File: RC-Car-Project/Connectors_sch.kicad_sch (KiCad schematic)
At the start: 9 parts, among them J1 XT60-M, J2 XT60-M, J3 XT60-M, J4 XT60-M, J5 MCU_IF, J6 ANT_IF, J7 Conn_02x09_Odd_Even

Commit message: Started on the PCB
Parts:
- removed J1, J2, J3, J4: XT60-M, symbol XT60-M:XT60-M
- added J1, J2, J3, J4: Conn_01x02_Pin, Connector_AMASS:AMASS_XT60-M_1x02_P7.20mm_Vertical, symbol Connector:Conn_01x02_Pin
- added J10, J8, J9: Conn_01x02, Connector_JST:JST_XH_B2B-XH-AM_1x02_P2.50mm_Vertical, symbol Connector_Generic:Conn_01x02
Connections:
- net GND_BATT: now also J1.1 (Pin_1), J2.1 (Pin_1)
- net LIGHTS1_NEG: now also J8.2 (Pin_2)
- net LIGHTS1_POS: now also J8.1 (Pin_1)
- net LIGHTS2_NEG: now also J9.2 (Pin_2)
- net LIGHTS2_POS: now also J9.1 (Pin_1)
- net M1_LEFT: now also J4.1 (Pin_1)
- net M1_RIGHT: now also J4.2 (Pin_2)
- net M2_LEFT: now also J3.1 (Pin_1)
- net M2_RIGHT: now also J3.2 (Pin_2)
- net THERMO1: now also J10.1 (Pin_1)
- net THERMO2: now also J10.2 (Pin_2)
- net VDD_BATT: now also J1.2 (Pin_2), J2.2 (Pin_2)

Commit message: Fixed Drivers
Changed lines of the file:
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@@
-		)
-	)
-	(hierarchical_label "RELAY_CTRL"
-		(shape input)
-		(at 196.85 86.36 180)
-		(fields_autoplaced yes)
-		(effects
-			(font
-				(size 1.27 1.27)
-			)
-			(justify right)
 		)
 	)

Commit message: Fixed Annotations
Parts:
- R3: renamed from R26; footprint Resistor_SMD:R_0201_0603Metric -> Resistor_SMD:R_0603_1608Metric
- R4: renamed from R25; footprint Resistor_SMD:R_0201_0603Metric -> Resistor_SMD:R_0603_1608Metric
- renumbered J6 to J10, J8 to J6, J9 to J7, J10 to J8, J7 to J9
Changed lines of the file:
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@@
 		(on_board yes)
 		(dnp no)
-		(property "Reference" "#PWR0104"
+		(property "Reference" "#PWR018"
 			(at 142.24 40.64 0)
 			(effects
@@
 			(project "RC-Car-Project"
 				(path "/ba870fd1-751d-4755-8e1a-1ea86ca9e2f6/47812da9-b622-4bda-8507-4e09448e1ff5"
-					(reference "#PWR0104")
+					(reference "#PWR018")
 					(unit 1)
 				)
@@
 		(dnp no)
 		(fields_autoplaced yes)
-		(property "Reference" "#PWR09"
+		(property "Reference" "#PWR015"
 			(at 127 92.71 0)
 			(effects
@@
 			(project "RC-Car-Project"
 				(path "/ba870fd1-751d-4755-8e1a-1ea86ca9e2f6/47812da9-b622-4bda-8507-4e09448e1ff5"
-					(reference "#PWR09")
+					(reference "#PWR015")
 					(unit 1)
 				)
@@
 		(on_board yes)
 		(dnp no)
-		(property "Reference" "#PWR012"
+		(property "Reference" "#PWR017"
 			(at 144.78 77.47 0)
 			(effects
@@
 			(project "RC-Car-Project"
 				(path "/ba870fd1-751d-4755-8e1a-1ea86ca9e2f6/47812da9-b622-4bda-8507-4e09448e1ff5"
-					(reference "#PWR012")
+					(reference "#PWR017")
 					(unit 1)
 				)
@@
 		(dnp no)
 		(fields_autoplaced yes)
-		(property "Reference" "J10"
+		(property "Reference" "J8"
 			(at 137.16 138.4299 0)
 			(effects
@@
 			(project "RC-Car-Project"
 				(path "/ba870fd1-751d-4755-8e1a-1ea86ca9e2f6/47812da9-b622-4bda-8507-4e09448e1ff5"
-					(reference "J10")
+					(reference "J8")
 					(unit 1)
 				)
@@
 		(dnp no)
 		(fields_autoplaced yes)
-		(property "Reference" "#PWR095"
+		(property "Reference" "#PWR014"
 			(at 67.31 104.14 0)
 			(effects
@@
 			(project "RC-Car-Project"
 				(path "/ba870fd1-751d-4755-8e1a-1ea86ca9e2f6/47812da9-b622-4bda-8507-4e09448e1ff5"
-					(reference "#PWR095")
+					(reference "#PWR014")
 					(unit 1)
 				)
@@
 		(dnp no)
 		(fields_autoplaced yes)
-		(property "Reference" "#PWR013"
+		(property "Reference" "#PWR020"
 			(at 165.1 67.31 0)
 			(effects
@@
 			(project "RC-Car-Project"
 				(path "/ba870fd1-751d-4755-8e1a-1ea86ca9e2f6/47812da9-b622-4bda-8507-4e09448e1ff5"
-					(reference "#PWR013")
+					(reference "#PWR020")
 					(unit 1)
 				)
@@
 		(dnp no)
 		(fields_autoplaced yes)
-		(property "Reference" "#PWR0105"
+		(property "Reference" "#PWR019"
 			(at 157.48 40.64 0)
 			(effects
@@
 			(project "RC-Car-Project"
 				(path "/ba870fd1-751d-4755-8e1a-1ea86ca9e2f6/47812da9-b622-4bda-8507-4e09448e1ff5"
-					(reference "#PWR0105")
+					(reference "#PWR019")
 					(unit 1)
 				)
@@
 		(dnp no)
 		(fields_autoplaced yes)
-		(property "Reference" "J8"
+		(property "Reference" "J6"
 			(at 137.16 123.1899 0)
 			(effects
@@
 			(project ""
 				(path "/ba870fd1-751d-4755-8e1a-1ea86ca9e2f6/47812da9-b622-4bda-8507-4e09448e1ff5"
-					(reference "J8")
+					(reference "J6")
 					(unit 1)
 				)
@@
 		(dnp no)
 		(fields_autoplaced yes)
-		(property "Reference" "J7"
+		(property "Reference" "J9"
 			(at 154.94 34.29 0)
 			(effects
@@
 			(project ""
 				(path "/ba870fd1-751d-4755-8e1a-1ea86ca9e2f6/47812da9-b622-4bda-8507-4e09448e1ff5"
-					(reference "J7")
+					(reference "J9")
 					(unit 1)
 				)
@@
 		(dnp no)
 		(fields_autoplaced yes)
-		(property "Reference" "#PWR08"
+		(property "Reference" "#PWR016"
 			(at 116.84 95.25 0)
 			(effects
@@
 			(project "RC-Car-Project"
 				(path "/ba870fd1-751d-4755-8e1a-1ea86ca9e2f6/47812da9-b622-4bda-8507-4e09448e1ff5"
-					(reference "#PWR08")
+					(reference "#PWR016")
 					(unit 1)
 				)
@@
 		(dnp no)
 		(fields_autoplaced yes)
-		(property "Reference" "#PWR092"
+		(property "Reference" "#PWR011"
 			(at 77.47 92.71 0)
 			(effects
@@
 			(project "RC-Car-Project"
 				(path "/ba870fd1-751d-4755-8e1a-1ea86ca9e2f6/47812da9-b622-4bda-8507-4e09448e1ff5"
-					(reference "#PWR092")
+					(reference "#PWR011")
 					(unit 1)
 				)
@@
 		(dnp no)
 		(fields_autoplaced yes)
-		(property "Reference" "#PWR094"
+		(property "Reference" "#PWR013"
 			(at 77.47 101.6 0)
 			(effects
@@
 			(project "RC-Car-Project"
 				(path "/ba870fd1-751d-4755-8e1a-1ea86ca9e2f6/47812da9-b622-4bda-8507-4e09448e1ff5"
-					(reference "#PWR094")
+					(reference "#PWR013")
 					(unit 1)
 				)
@@
 		(dnp no)
 		(fields_autoplaced yes)
-		(property "Reference" "#PWR093"
+		(property "Reference" "#PWR012"
 			(at 67.31 95.25 0)
 			(effects
@@
 			(project "RC-Car-Project"
 				(path "/ba870fd1-751d-4755-8e1a-1ea86ca9e2f6/47812da9-b622-4bda-8507-4e09448e1ff5"
-					(reference "#PWR093")
+					(reference "#PWR012")
 					(unit 1)
 				)
@@
 		(dnp no)
 		(fields_autoplaced yes)
-		(property "Reference" "J9"
+		(property "Reference" "J7"
 			(at 137.16 130.8099 0)
 			(effects
@@
 			(project "RC-Car-Project"
 				(path "/ba870fd1-751d-4755-8e1a-1ea86ca9e2f6/47812da9-b622-4bda-8507-4e09448e1ff5"
-					(reference "J9")
+					(reference "J7")
 					(unit 1)
 				)
@@
 		(dnp no)
 		(fields_autoplaced yes)
-		(property "Reference" "R25"
+		(property "Reference" "R4"
 			(at 167.64 66.0399 0)
 			(effects
@@
 			)
 		)
-		(property "Footprint" "Resistor_SMD:R_0201_0603Metric"
+		(property "Footprint" "Resistor_SMD:R_0603_1608Metric"
 			(at 166.878 67.31 90)
 			(effects
@@
 			(project "RC-Car-Project"
 				(path "/ba870fd1-751d-4755-8e1a-1ea86ca9e2f6/47812da9-b622-4bda-8507-4e09448e1ff5"
-					(reference "R25")
+					(reference "R4")
 					(unit 1)
 				)
@@
 		(dnp no)
 		(fields_autoplaced yes)
-		(property "Reference" "#PWR091"
+		(property "Reference" "#PWR021"
 			(at 187.96 99.06 0)
 			(effects
@@
 			(project "RC-Car-Project"
 				(path "/ba870fd1-751d-4755-8e1a-1ea86ca9e2f6/47812da9-b622-4bda-8507-4e09448e1ff5"
-					(reference "#PWR091")
+					(reference "#PWR021")
 					(unit 1)
 				)
@@
 		(dnp no)
 		(fields_autoplaced yes)
-		(property "Reference" "J6"
+		(property "Reference" "J10"
 			(at 178.5504 92.71 0)
 			(effects
@@
 			(project ""
 				(path "/ba870fd1-751d-4755-8e1a-1ea86ca9e2f6/47812da9-b622-4bda-8507-4e09448e1ff5"
-					(reference "J6")
+					(reference "J10")
 					(unit 1)
 				)
@@
 		(dnp no)
 		(fields_autoplaced yes)
-		(property "Reference" "R26"
+		(property "Reference" "R3"
 			(at 147.32 66.0399 0)
 			(effects
@@
 			)
 		)
-		(property "Footprint" "Resistor_SMD:R_0201_0603Metric"
+		(property "Footprint" "Resistor_SMD:R_0603_1608Metric"
 			(at 146.558 67.31 90)
 			(effects
@@
 			(project "RC-Car-Project"
 				(path "/ba870fd1-751d-4755-8e1a-1ea86ca9e2f6/47812da9-b622-4bda-8507-4e09448e1ff5"
-					(reference "R26")
-					(unit 1)
-				)
+					(reference "R3")
+					(unit 1)
+				)

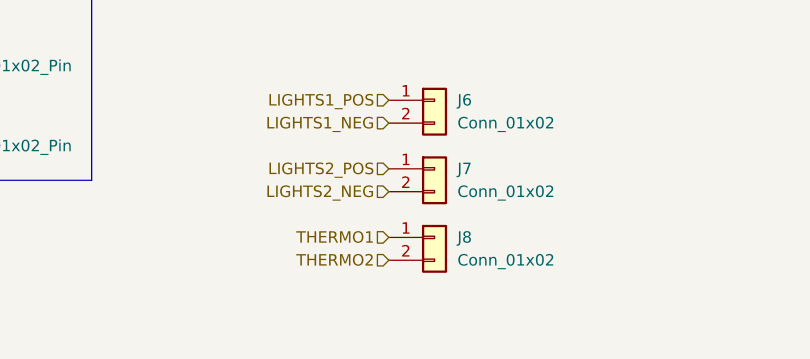
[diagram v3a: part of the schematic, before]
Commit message: Add RF filter + another thermo header + layout everything
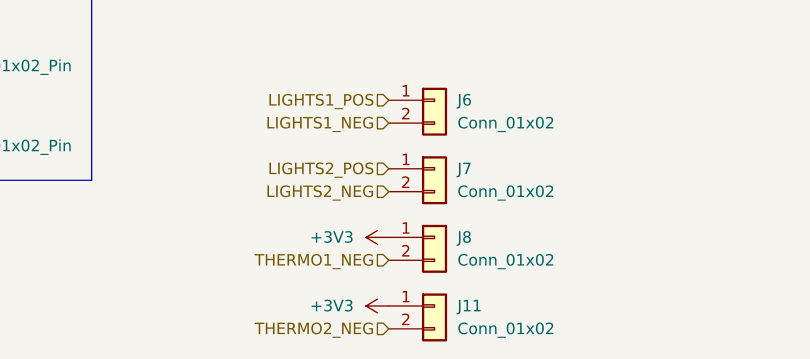
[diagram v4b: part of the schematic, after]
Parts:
- added J11: Conn_01x02, Connector_JST:JST_XH_B2B-XH-AM_1x02_P2.50mm_Vertical, symbol Connector_Generic:Conn_01x02
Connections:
- net THERMO1 is gone; now on net +3V3: J8.1 (Pin_1)
- net +3V3: now also J11.1 (Pin_1)
- net THERMO2 renamed THERMO1_NEG
- new net THERMO2_NEG: J11.2 (Pin_2)
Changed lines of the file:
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@@
+		)
+	)
+	(hierarchical_label "THERMO2_NEG"
+		(shape input)
+		(at 129.54 148.59 180)
+		(fields_autoplaced yes)
+		(effects
+			(font
+				(size 1.27 1.27)
+			)
+			(justify right)
 		)
 	)
@@
 		)
 	)
-	(hierarchical_label "THERMO1"
-		(shape input)
-		(at 129.54 138.43 180)
+	(hierarchical_label "I2C2_CAM_SDA"
+		(shape input)
+		(at 148.59 43.18 180)
 		(fields_autoplaced yes)
 		(effects
@@
 		)
 	)
-	(hierarchical_label "I2C2_CAM_SDA"
-		(shape input)
-		(at 148.59 43.18 180)
+	(hierarchical_label "RF_ANT"
+		(shape input)
+		(at 176.53 99.06 180)
 		(fields_autoplaced yes)
 		(effects
@@
 		)
 	)
-	(hierarchical_label "RF_ANT"
-		(shape input)
-		(at 176.53 99.06 180)
+	(hierarchical_label "LIGHTS1_POS"
+		(shape input)
+		(at 129.54 123.19 180)
 		(fields_autoplaced yes)
 		(effects
@@
 		)
 	)
-	(hierarchical_label "LIGHTS1_POS"
-		(shape input)
-		(at 129.54 123.19 180)
+	(hierarchical_label "LIGHTS2_POS"
+		(shape input)
+		(at 129.54 130.81 180)
 		(fields_autoplaced yes)
 		(effects
@@
 		)
 	)
-	(hierarchical_label "LIGHTS2_POS"
-		(shape input)
-		(at 129.54 130.81 180)
+	(hierarchical_label "USART_TX"
+		(shape input)
+		(at 123.19 107.95 180)
 		(fields_autoplaced yes)
 		(effects
@@
 		)
 	)
-	(hierarchical_label "USART_TX"
-		(shape input)
-		(at 123.19 107.95 180)
+	(hierarchical_label "SWDIO"
+		(shape input)
+		(at 123.19 100.33 180)
 		(fields_autoplaced yes)
 		(effects
@@
 		)
 	)
-	(hierarchical_label "SWDIO"
-		(shape input)
-		(at 123.19 100.33 180)
+	(hierarchical_label "M2_RIGHT"
+		(shape input)
+		(at 73.66 116.84 180)
 		(fields_autoplaced yes)
 		(effects
@@
 		)
 	)
-	(hierarchical_label "M2_RIGHT"
-		(shape input)
-		(at 73.66 116.84 180)
-		(fields_autoplaced yes)
-		(effects
-			(font
-				(size 1.27 1.27)
-			)
-			(justify right)
-		)
-	)
-	(hierarchical_label "THERMO2"
+	(hierarchical_label "THERMO1_NEG"
 		(shape input)
 		(at 129.54 140.97 180)
@@
 	(symbol
 		(lib_id "Connector_Generic:Conn_01x02")
+		(at 134.62 146.05 0)
+		(unit 1)
+		(exclude_from_sim no)
+		(in_bom yes)
+		(on_board yes)
+		(dnp no)
+		(fields_autoplaced yes)
+		(property "Reference" "J11"
+			(at 137.16 146.0499 0)
+			(effects
+				(font
+					(size 1.27 1.27)
+				)
+				(justify left)
+			)
+		)
+		(property "Value" "Conn_01x02"
+			(at 137.16 148.5899 0)
+			(effects
+				(font
+					(size 1.27 1.27)
+				)
+				(justify left)
+			)
+		)
+		(property "Footprint" "Connector_JST:JST_XH_B2B-XH-AM_1x02_P2.50mm_Vertical"
+			(at 134.62 146.05 0)
+			(effects
+				(font
+					(size 1.27 1.27)
+				)
+				(hide yes)
+			)
+		)
+		(property "Datasheet" "~"
+			(at 134.62 146.05 0)
+			(effects
+				(font
+					(size 1.27 1.27)
+				)
+				(hide yes)
+			)
+		)
+		(property "Description" "Generic connector, single row, 01x02, script generated (kicad-library-utils/schlib/autogen/connector/)"
+			(at 134.62 146.05 0)
+			(effects
+				(font
+					(size 1.27 1.27)
+				)
+				(hide yes)
+			)
+		)
+		(pin "1"
+		)
+		(pin "2"
+		)
+		(instances
+			(project "RC-Car-Project"
+				(path "/ba870fd1-751d-4755-8e1a-1ea86ca9e2f6/47812da9-b622-4bda-8507-4e09448e1ff5"
+					(reference "J11")
+					(unit 1)
+				)
+			)
+		)
+	)
+	(symbol
+		(lib_id "Connector_Generic:Conn_01x02")
 		(at 134.62 138.43 0)
 		(unit 1)
@@
 	(symbol
 		(lib_id "power:+3V3")
+		(at 129.54 146.05 90)
+		(unit 1)
+		(exclude_from_sim no)
+		(in_bom yes)
+		(on_board yes)
+		(dnp no)
+		(fields_autoplaced yes)
+		(property "Reference" "#PWR0132"
+			(at 133.35 146.05 0)
+			(effects
+				(font
+					(size 1.27 1.27)
+				)
+				(hide yes)
+			)
+		)
+		(property "Value" "+3V3"
+			(at 125.65 146.0499 90)
+			(effects
+				(font
+					(size 1.27 1.27)
+				)
+				(justify left)
+			)
+		)
+		(property "Footprint" ""
+			(at 129.54 146.05 0)
+			(effects
+				(font
+					(size 1.27 1.27)
+				)
+				(hide yes)
+			)
+		)
+		(property "Datasheet" ""
+			(at 129.54 146.05 0)
+			(effects
+				(font
+					(size 1.27 1.27)
+				)
+				(hide yes)
+			)
+		)
+		(property "Description" "Power symbol creates a global label with name \"+3V3\""
+			(at 129.54 146.05 0)
+			(effects
+				(font
+					(size 1.27 1.27)
+				)
+				(hide yes)
+			)
+		)
+		(pin "1"
+		)
+		(instances
+			(project "RC-Car-Project"
+				(path "/ba870fd1-751d-4755-8e1a-1ea86ca9e2f6/47812da9-b622-4bda-8507-4e09448e1ff5"
+					(reference "#PWR0132")
+					(unit 1)
+				)
+			)
+		)
+	)
+	(symbol
+		(lib_id "power:+3V3")
 		(at 165.1 71.12 180)
 		(unit 1)
@@
 					(unit 1)
 				)
+			)
+		)
+	)
+	(symbol
+		(lib_id "power:+3V3")
+		(at 129.54 138.43 90)
+		(unit 1)
+		(exclude_from_sim no)
+		(in_bom yes)
+		(on_board yes)
+		(dnp no)
+		(fields_autoplaced yes)
+		(property "Reference" "#PWR0131"
+			(at 133.35 138.43 0)
+			(effects
+				(font
+					(size 1.27 1.27)
+				)
+				(hide yes)
+			)
+		)
+		(property "Value" "+3V3"
+			(at 125.65 138.4299 90)
+			(effects
+				(font
+					(size 1.27 1.27)
+				)
+				(justify left)
+			)
+		)
+		(property "Footprint" ""
+			(at 129.54 138.43 0)
+			(effects
+				(font
+					(size 1.27 1.27)
+				)
+				(hide yes)
+			)
+		)
+		(property "Datasheet" ""
+			(at 129.54 138.43 0)
+			(effects
+				(font
+					(size 1.27 1.27)
+				)
+				(hide yes)
+			)
+		)
+		(property "Description" "Power symbol creates a global label with name \"+3V3\""
+			(at 129.54 138.43 0)
+			(effects
+				(font
+					(size 1.27 1.27)
+				)
+				(hide yes)
+			)
+		)
+		(pin "1"
+		)
+		(instances
+			(project "RC-Car-Project"
+				(path "/ba870fd1-751d-4755-8e1a-1ea86ca9e2f6/47812da9-b622-4bda-8507-4e09448e1ff5"
+					(reference "#PWR0131")
+					(unit 1)
+				)

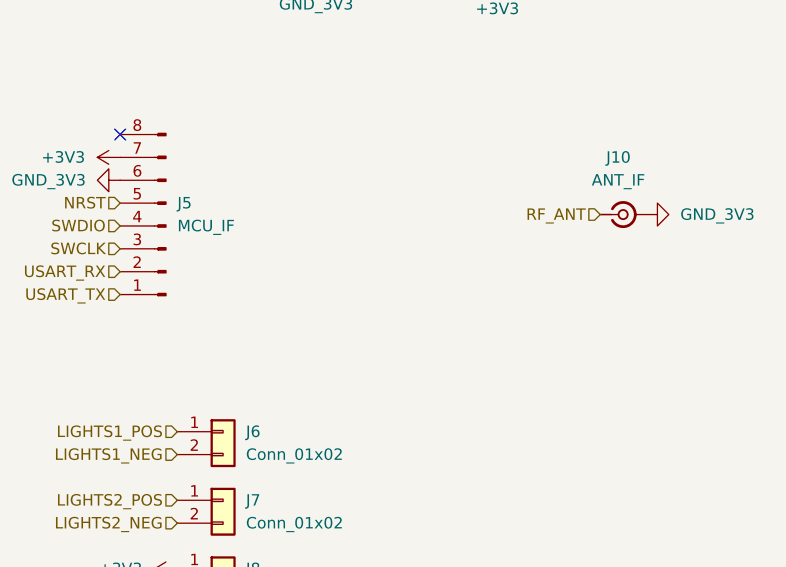
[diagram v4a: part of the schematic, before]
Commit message: Add switch
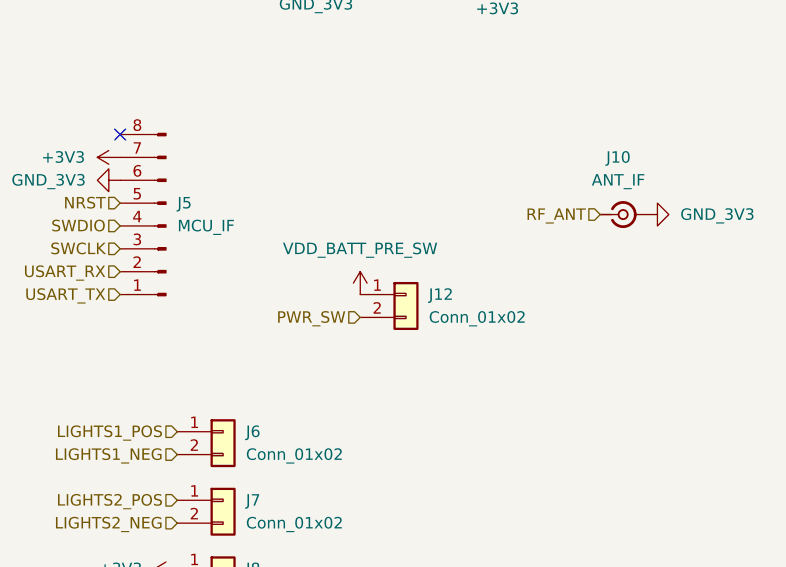
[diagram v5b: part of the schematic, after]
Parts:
- added J12: Conn_01x02, Connector_JST:JST_XH_B2B-XH-AM_1x02_P2.50mm_Vertical, symbol Connector_Generic:Conn_01x02
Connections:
- new net PWR_SW: J12.2 (Pin_2)
- new net VDD_BATT_PRE_SW: J12.1 (Pin_1)
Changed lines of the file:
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@@
+		)
+	)
+	(hierarchical_label "PWR_SW"
+		(shape input)
+		(at 149.86 110.49 180)
+		(fields_autoplaced yes)
+		(effects
+			(font
+				(size 1.27 1.27)
+			)
+			(justify right)
 		)
 	)
@@
 	)
 	(symbol
+		(lib_id "Connector_Generic:Conn_01x02")
+		(at 154.94 107.95 0)
+		(unit 1)
+		(exclude_from_sim no)
+		(in_bom yes)
+		(on_board yes)
+		(dnp no)
+		(fields_autoplaced yes)
+		(property "Reference" "J12"
+			(at 157.48 107.9499 0)
+			(effects
+				(font
+					(size 1.27 1.27)
+				)
+				(justify left)
+			)
+		)
+		(property "Value" "Conn_01x02"
+			(at 157.48 110.4899 0)
+			(effects
+				(font
+					(size 1.27 1.27)
+				)
+				(justify left)
+			)
+		)
+		(property "Footprint" "Connector_JST:JST_XH_B2B-XH-AM_1x02_P2.50mm_Vertical"
+			(at 154.94 107.95 0)
+			(effects
+				(font
+					(size 1.27 1.27)
+				)
+				(hide yes)
+			)
+		)
+		(property "Datasheet" "~"
+			(at 154.94 107.95 0)
+			(effects
+				(font
+					(size 1.27 1.27)
+				)
+				(hide yes)
+			)
+		)
+		(property "Description" "Generic connector, single row, 01x02, script generated (kicad-library-utils/schlib/autogen/connector/)"
+			(at 154.94 107.95 0)
+			(effects
+				(font
+					(size 1.27 1.27)
+				)
+				(hide yes)
+			)
+		)
+		(pin "1"
+		)
+		(pin "2"
+		)
+		(instances
+			(project "RC-Car-Project"
+				(path "/ba870fd1-751d-4755-8e1a-1ea86ca9e2f6/47812da9-b622-4bda-8507-4e09448e1ff5"
+					(reference "J12")
+					(unit 1)
+				)
+			)
+		)
+	)
+	(symbol
 		(lib_id "power:GND")
 		(at 73.66 95.25 270)
@@
 					(unit 1)
 				)
+			)
+		)
+	)
+	(symbol
+		(lib_id "power:+3V3")
+		(at 149.86 107.95 0)
+		(unit 1)
+		(exclude_from_sim no)
+		(in_bom yes)
+		(on_board yes)
+		(dnp no)
+		(fields_autoplaced yes)
+		(property "Reference" "#PWR0136"
+			(at 149.86 111.76 0)
+			(effects
+				(font
+					(size 1.27 1.27)
+				)
+				(hide yes)
+			)
+		)
+		(property "Value" "VDD_BATT_PRE_SW"
+			(at 149.86 102.87 0)
+			(effects
+				(font
+					(size 1.27 1.27)
+				)
+			)
+		)
+		(property "Footprint" ""
+			(at 149.86 107.95 0)
+			(effects
+				(font
+					(size 1.27 1.27)
+				)
+				(hide yes)
+			)
+		)
+		(property "Datasheet" ""
+			(at 149.86 107.95 0)
+			(effects
+				(font
+					(size 1.27 1.27)
+				)
+				(hide yes)
+			)
+		)
+		(property "Description" "Power symbol creates a global label with name \"+3V3\""
+			(at 149.86 107.95 0)
+			(effects
+				(font
+					(size 1.27 1.27)
+				)
+				(hide yes)
+			)
+		)
+		(pin "1"
+		)
+		(instances
+			(project "RC-Car-Project"
+				(path "/ba870fd1-751d-4755-8e1a-1ea86ca9e2f6/47812da9-b622-4bda-8507-4e09448e1ff5"
+					(reference "#PWR0136")
+					(unit 1)
+				)
